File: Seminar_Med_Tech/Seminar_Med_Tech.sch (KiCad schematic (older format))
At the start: 21 parts

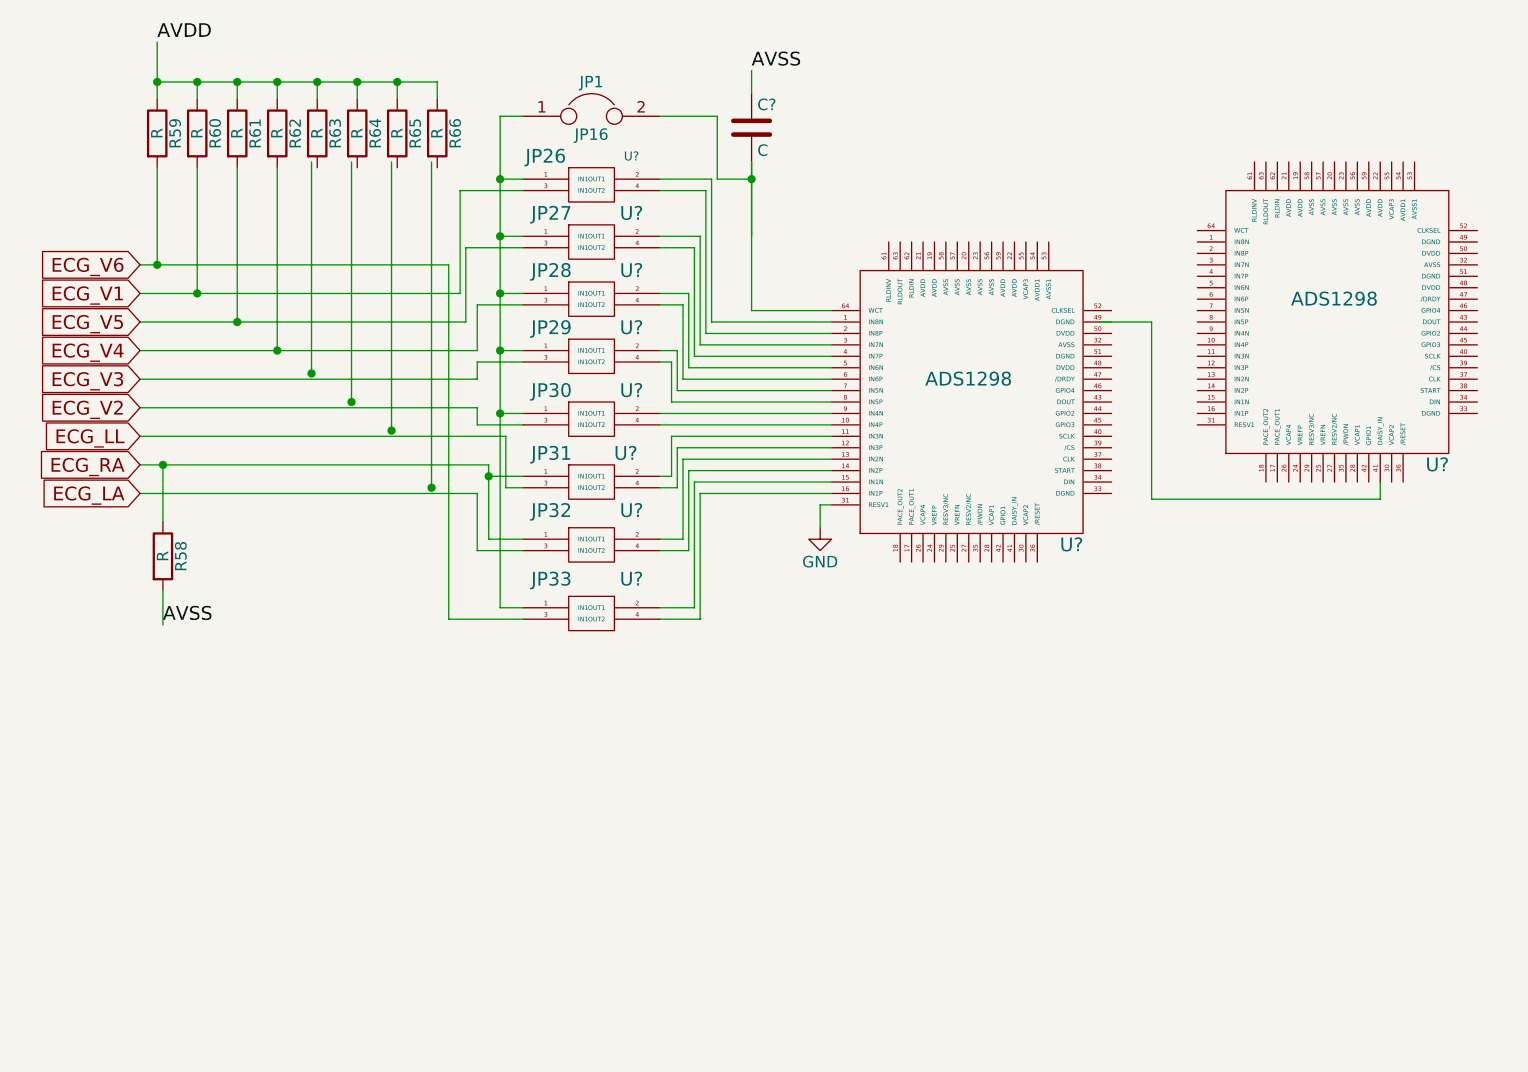
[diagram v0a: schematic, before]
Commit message: Modified Circuit schema
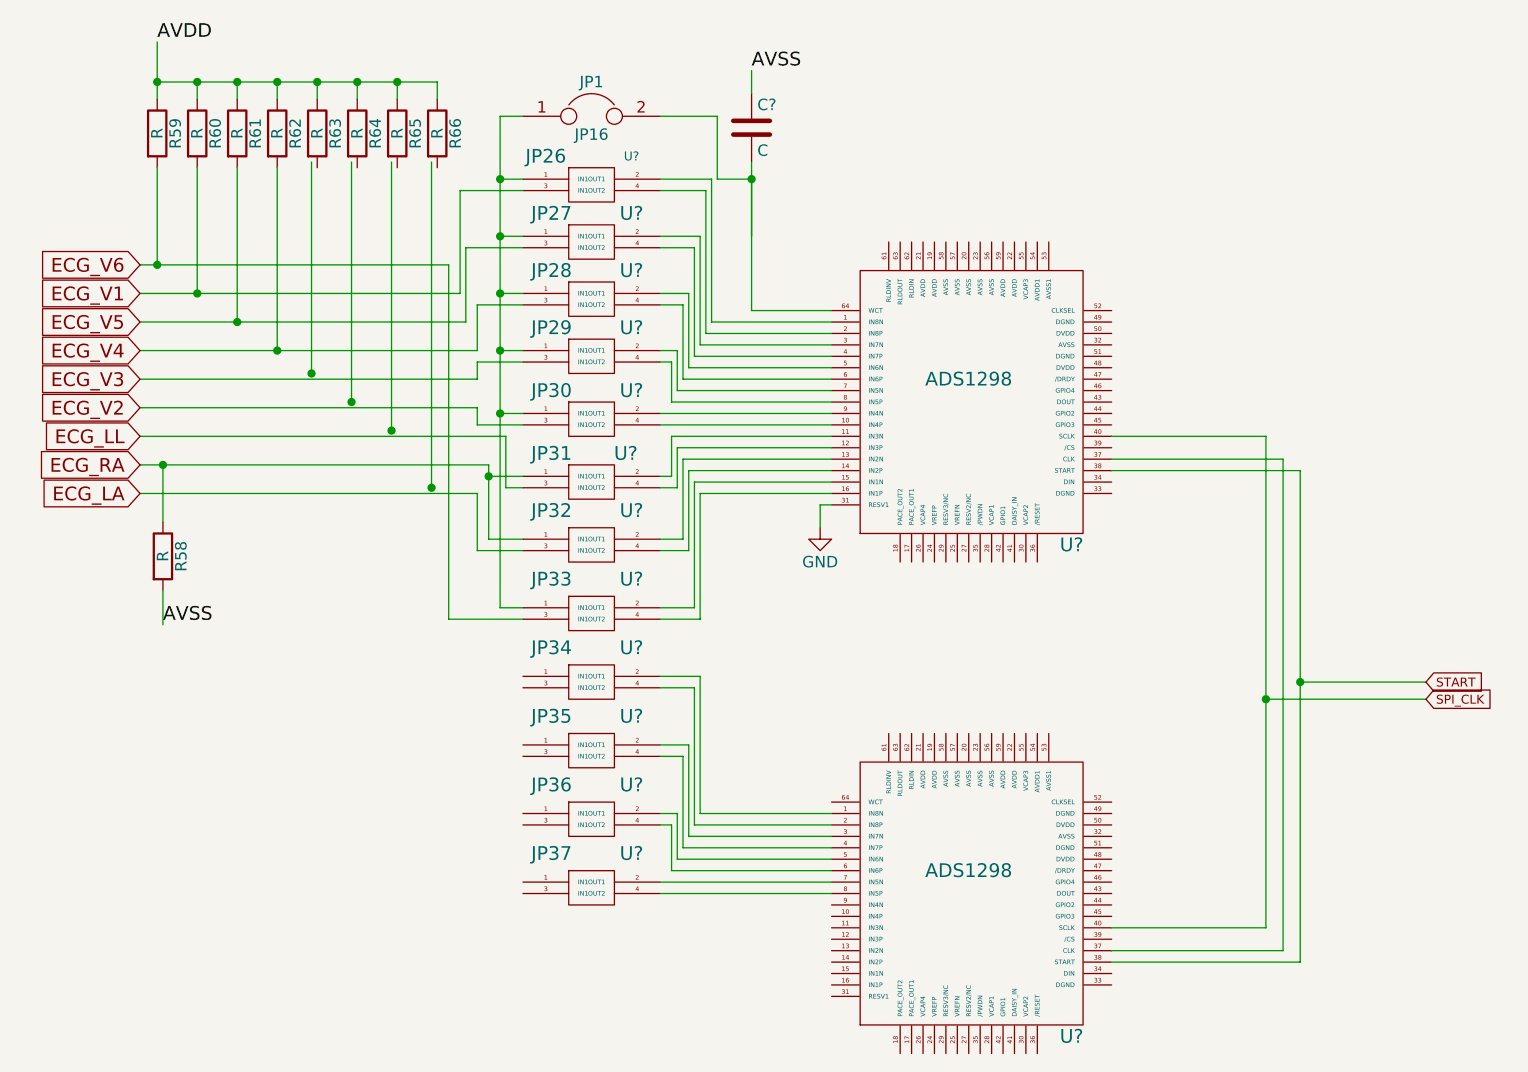
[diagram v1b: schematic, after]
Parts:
- added U?: JP34, symbol Jumper2x2
- added U?: JP35, symbol Jumper2x2
- added U?: JP36, symbol Jumper2x2
- added U?: JP37, symbol Jumper2x2
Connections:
- net labels added: SPI_CLK, START
- wire segments 112 -> 139
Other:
- moved on the sheet: U?
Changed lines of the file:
@@
 L ADS1298 U?
 U 1 1 592207CE
-P 6300 3150
-F 0 "U?" H 6750 2525 60  0000 C CNN
-F 1 "ADS1298" H 6300 3250 60  0000 C CNN
-F 2 "" H 6250 3000 60  0001 C CNN
-F 3 "" H 6250 3000 60  0001 C CNN
-	1    6300 3150
+P 4700 5650
+F 0 "U?" H 5150 5025 60  0000 C CNN
+F 1 "ADS1298" H 4700 5750 60  0000 C CNN
+F 2 "" H 4650 5500 60  0001 C CNN
+F 3 "" H 4650 5500 60  0001 C CNN
+	1    4700 5650
 	1    0    0    -1
 $EndComp
@@
 	2750 4450 2425 4450
 Wire Wire Line
-	2425 4450 2425 2900
-Wire Wire Line
-	2425 2900 1075 2900
+	2425 2900 2425 4450
+Wire Wire Line
+	1075 2900 2425 2900
 Wire Wire Line
 	1075 3025 2475 3025
@@
 	2750 2825 2500 2825
 Wire Wire Line
-	2500 2825 2500 3150
-Wire Wire Line
-	2500 3150 1075 3150
+	2500 3150 2500 2825
+Wire Wire Line
+	1075 3150 2500 3150
 Wire Wire Line
 	1075 3275 2550 3275
@@
 	3750 2450 3750 3100
 Wire Wire Line
-	3750 2450 3750 2775
+	3750 2525 3750 2775
 Wire Wire Line
 	3600 2525 3750 2525
-Wire Wire Line
-	5275 3150 5500 3150
-Wire Wire Line
-	5500 3150 5500 3925
-Wire Wire Line
-	6500 3850 6500 3925
-Wire Wire Line
-	6500 3925 5500 3925
 Wire Wire Line
 	3750 3100 4100 3100
@@
 Wire Wire Line
 	4050 3950 4050 4050
+$Comp
+L Jumper2x2 U?
+U 1 1 5924BCF7
+P 3050 4725
+F 0 "U?" H 3225 4875 60  0000 C CNN
+F 1 "JP34" H 2875 4875 60  0000 C CNN
+F 2 "" H 3125 4725 60  0001 C CNN
+F 3 "" H 3125 4725 60  0001 C CNN
+	1    3050 4725
+	1    0    0    -1
+$EndComp
+$Comp
+L Jumper2x2 U?
+U 1 1 5924BDFA
+P 3050 5025
+F 0 "U?" H 3225 5175 60  0000 C CNN
+F 1 "JP35" H 2875 5175 60  0000 C CNN
+F 2 "" H 3125 5025 60  0001 C CNN
+F 3 "" H 3125 5025 60  0001 C CNN
+	1    3050 5025
+	1    0    0    -1
+$EndComp
+$Comp
+L Jumper2x2 U?
+U 1 1 5924BE51
+P 3050 5325
+F 0 "U?" H 3225 5475 60  0000 C CNN
+F 1 "JP36" H 2875 5475 60  0000 C CNN
+F 2 "" H 3125 5325 60  0001 C CNN
+F 3 "" H 3125 5325 60  0001 C CNN
+	1    3050 5325
+	1    0    0    -1
+$EndComp
+$Comp
+L Jumper2x2 U?
+U 1 1 5924CBE4
+P 3050 5625
+F 0 "U?" H 3225 5775 60  0000 C CNN
+F 1 "JP37" H 2875 5775 60  0000 C CNN
+F 2 "" H 3125 5625 60  0001 C CNN
+F 3 "" H 3125 5625 60  0001 C CNN
+	1    3050 5625
+	1    0    0    -1
+$EndComp
+Wire Wire Line
+	5325 3800 6150 3800
+Wire Wire Line
+	6150 3800 6150 5950
+Wire Wire Line
+	6150 5950 5325 5950
+Wire Wire Line
+	6150 4725 6700 4725
+Connection ~ 6150 4725
+Text GLabel 6700 4725 2    39   Input ~ 0
+START
+Wire Wire Line
+	5325 3750 6075 3750
+Wire Wire Line
+	6075 5900 5325 5900
+Wire Wire Line
+	3525 5300 4100 5300
+Wire Wire Line
+	3500 5350 4100 5350
+Wire Wire Line
+	3475 5400 4100 5400
+Wire Wire Line
+	3450 5450 4100 5450
+Wire Wire Line
+	3425 5500 4100 5500
+Wire Wire Line
+	3400 5550 4100 5550
+Wire Wire Line
+	4100 5600 3350 5600
+Wire Wire Line
+	3350 5650 4100 5650
+Wire Wire Line
+	3350 5350 3400 5350
+Wire Wire Line
+	3400 5350 3400 5550
+Wire Wire Line
+	3425 5500 3425 5300
+Wire Wire Line
+	3425 5300 3350 5300
+Wire Wire Line
+	3350 5050 3450 5050
+Wire Wire Line
+	3450 5050 3450 5450
+Wire Wire Line
+	3475 5400 3475 5000
+Wire Wire Line
+	3475 5000 3350 5000
+Wire Wire Line
+	3350 4750 3500 4750
+Wire Wire Line
+	3500 4750 3500 5350
+Wire Wire Line
+	3525 5300 3525 4700
+Wire Wire Line
+	3525 4700 3350 4700
+Wire Wire Line
+	6000 5800 5325 5800
+Wire Wire Line
+	6000 3650 6000 5800
+Wire Wire Line
+	6000 3650 5325 3650
+Wire Wire Line
+	6000 4800 6700 4800
+Connection ~ 6000 4800
+Text GLabel 6700 4800 2    39   Input ~ 0
+SPI_CLK
+Wire Wire Line
+	6075 3750 6075 5900
 $EndSCHEMATC

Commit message: Tried to cascade the two chips
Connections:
- net labels added: CLK, SPI_CS0, SPI_CS1, SPI_IN, SPI_OUT, SPI_START
- net labels removed: START
- wire segments 139 -> 150

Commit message: Updated Schaltplan
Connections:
- wire segments 150 -> 156
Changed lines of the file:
@@
 Text GLabel 6325 4700 2    39   Input ~ 0
 SPI_START
+Text Label 6675 4550 2    39   ~ 0
+CLK
 Wire Wire Line
 	1150 1925 1150 2175
@@
 Connection ~ 1675 3275
 Wire Wire Line
-	1825 2450 1825 3375
-Connection ~ 1825 3375
-Wire Wire Line
-	2000 2450 2000 3500
-Connection ~ 2000 3500
-Wire Wire Line
-	2175 2450 2175 3625
-Connection ~ 2175 3625
-Wire Wire Line
-	2350 2450 2350 3875
-Connection ~ 2350 3875
+	1825 2450 1825 3400
+Connection ~ 1825 3400
+Wire Wire Line
+	2000 2450 2000 3525
+Connection ~ 2000 3525
+Wire Wire Line
+	2175 2450 2175 3650
+Connection ~ 2175 3650
+Wire Wire Line
+	2350 2450 2350 3900
+Connection ~ 2350 3900
 Wire Wire Line
 	1175 4325 1175 4475
@@
 	1075 3775 2600 3775
 Wire Wire Line
-	2675 3650 2675 3875
+	2675 3650 2675 4750
 Wire Wire Line
 	2675 3875 2750 3875
@@
 	1075 3900 2550 3900
 Wire Wire Line
-	2550 3900 2550 4150
+	2550 3900 2550 4700
 Wire Wire Line
 	2600 3775 2600 4100
@@
 	3750 2450 3750 3100
 Wire Wire Line
-	3750 2525 3750 2775
-Wire Wire Line
 	3600 2525 3750 2525
 Wire Wire Line
@@
 	5325 6000 5725 6000
 Wire Wire Line
-	5725 6000 5725 3850
+	5725 6000 5725 4775
+Wire Wire Line
+	5875 4775 5875 3850
 Wire Wire Line
 	5725 3850 5325 3850
 Wire Wire Line
-	5925 5650 5925 3500
-Wire Wire Line
-	5875 5800 5875 3650
+	5925 5650 5925 4350
+Wire Wire Line
+	6075 4350 6075 3500
+Wire Wire Line
+	5875 5800 5875 4425
+Wire Wire Line
+	6025 4425 6025 3650
 Wire Wire Line
 	5925 3500 5325 3500
@@
 	5325 3700 6325 3700
 Wire Wire Line
-	6325 4775 5725 4775
+	5725 4775 6325 4775
 Connection ~ 5725 4775
 Wire Wire Line
-	6325 4425 5875 4425
+	5875 4425 6325 4425
 Connection ~ 5875 4425
 Wire Wire Line
-	6325 4350 5925 4350
+	5925 4350 6325 4350
 Connection ~ 5925 4350
 Wire Wire Line
 	5325 3800 5775 3800
 Wire Wire Line
-	5775 3800 5775 5950
+	5775 3800 5775 4700
+Wire Wire Line
+	5925 4700 5925 5950
 Wire Wire Line
 	5775 5950 5325 5950
@@
 	5325 3750 5825 3750
 Wire Wire Line
-	5825 3750 5825 5900
+	5825 3750 5825 4550
+Wire Wire Line
+	5975 4550 5975 5900
 Wire Wire Line
 	5825 5900 5325 5900
 Wire Wire Line
-	6325 4700 5775 4700
+	5775 4700 6325 4700
 Connection ~ 5775 4700
 Wire Wire Line
 	5825 4550 6975 4550
 Connection ~ 5825 4550
-Text Label 6675 4550 2    39   ~ 0
-CLK
+Wire Wire Line
+	2675 4750 2750 4750
+Connection ~ 2675 3875
+Wire Wire Line
+	2550 4700 2750 4700
+Connection ~ 2550 4150
 $EndSCHEMATC

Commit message: Updated Schaltbild
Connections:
- wire segments 156 -> 147
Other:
- moved on the sheet: C?, JP1, R63, R64, R65, R66, U?

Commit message: Updated Schaltbil
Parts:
- added C1, C2, C? (x2): 1uF, symbol C
- added C10, C?: 10uF, symbol C
- added C33, C?: Nl, symbol C
- added C9, C?: 22uF, symbol C
- added C95, C?: 0.1uF, symbol C
- added JP? (x2): Jumper, symbol Jumper
- added R6, R7, R? (x2): 10k, symbol R
- added TP3, TP?: TEST, symbol TEST
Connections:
- net labels added: /PWDN, /RESET, DAISY_IN, DVDD, GPIO11, GPIO21, PACEOUT11, PACEOUT12, PACEOUT21, PACEOUT22, ReservedIN1N, ReservedIN1P, ReservedIN2N, ReservedIN2P, ReservedIN3N, ReservedIN3P, ReservedIN4N, ReservedIN4P, VREFP
- net labels removed: SPI_CS1
- wire segments 147 -> 369
- no-connect marks 0 -> 5
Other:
- moved on the sheet: C?, JP1, R58, R59, R60, R61, R62, R63, R64, R65, R66, U?

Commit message: Updated Schaltbild
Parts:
- added TP1, TP11, TP12, TP2: TEST, symbol TEST
- added U?: J5, symbol Header12
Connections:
- net labels added: GPIO13, GPIO14, GPIO24
- wire segments 369 -> 327
- no-connect marks 5 -> 10
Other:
- moved on the sheet: U?

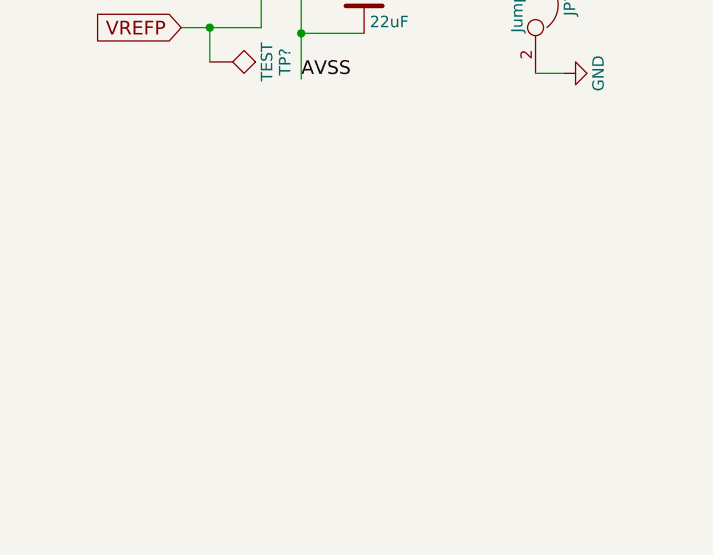
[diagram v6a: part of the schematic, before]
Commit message: Updated Dokumentation and added capacitors
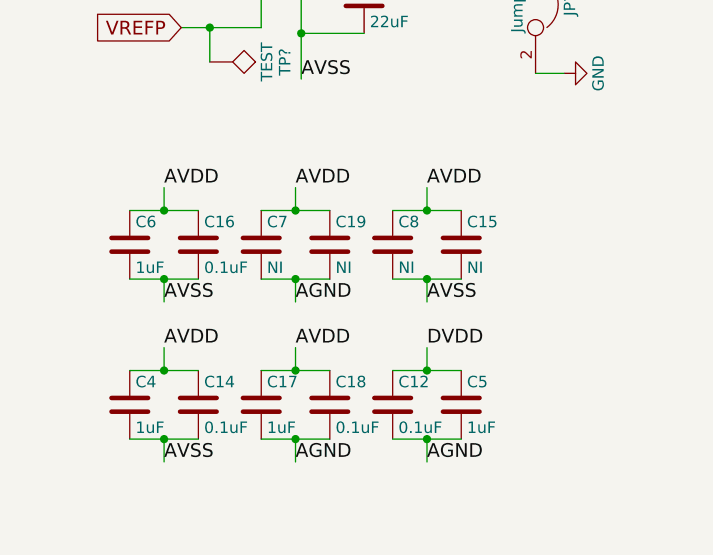
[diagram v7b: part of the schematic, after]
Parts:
- added C12, C14, C16, C18: 0.1uF, symbol C
- added C15, C19, C7, C8: NI, symbol C
- added C17, C4, C5, C6: 1uF, symbol C
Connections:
- net labels added: AGND
- wire segments 327 -> 351

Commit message: Added RLD
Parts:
- added C20: 0.01uF, symbol C
- added C21, C22: NI, symbol C
- added JP1: NI, symbol Jumper_NC_Small
- added JP17: NI, symbol Jumper_NC_Dual
- added R3: 0, symbol R
- added R4: NI, symbol R
- added R8: 392K, symbol R
- added U?: OPA2340, symbol OPA2340
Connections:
- net labels added: ECG_RL, ECG_SHD_DRV
- wire segments 351 -> 384
